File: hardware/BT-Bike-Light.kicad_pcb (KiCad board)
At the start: 2 copper layers, 0 parts

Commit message: Replace battery connector footprint and import footprints
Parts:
- added BT101: 18650, Keystone:254, F.Cu at (130.6, 129.6)
- added BZ101: Buzzer, PUI-Audio:PUI_AT-1220-TT-3V-2-R, F.Cu at (43.6, 112.8)
- added C101: 100nF, Capacitor_SMD:C_0402_1005Metric, F.Cu at (137.1, 86.0)
- added C102: 100nF, Capacitor_SMD:C_0402_1005Metric, F.Cu at (118.9, 100.1)
- added C103: 1uF, Capacitor_SMD:C_0402_1005Metric, F.Cu at (60.4, 123.1)
- added C104: 1uF, Capacitor_SMD:C_0402_1005Metric, F.Cu at (66.0, 123.1)
- added C201: 1uF, Capacitor_SMD:C_0402_1005Metric, F.Cu at (76.9, 75.0)
- added C202: 1uF, Capacitor_SMD:C_0402_1005Metric, F.Cu at (81.3, 75.0)
- added C301: 220nF, Capacitor_SMD:C_0402_1005Metric, F.Cu at (97.9, 95.0)
- added C302: 1uF, Capacitor_SMD:C_0402_1005Metric, F.Cu at (98.4, 96.6)
- added C401: 10uF, Capacitor_SMD:C_0402_1005Metric, F.Cu at (100.7, 116.2)
- added C402: 100nF, Capacitor_SMD:C_0402_1005Metric, F.Cu at (100.7, 115.1)
- added C403: 100nF, Capacitor_SMD:C_0402_1005Metric, F.Cu at (100.7, 114.0)
- added C501: 4.7uF, Capacitor_SMD:C_0402_1005Metric, F.Cu at (91.3, 76.3)
- added C502: 4.7uF, Capacitor_SMD:C_0402_1005Metric, F.Cu at (100.3, 75.9)
- added D501: RED, LED_SMD:LED_Cree-XP, F.Cu at (103.0, 77.0)
- added F101: 3A, Fuse:Fuse_1812_4532Metric, F.Cu at (85.5, 74.1)
- added J101: USB_C_Charge_Port, CUI-Devices:UJC-HP2-3-SMT-TR, F.Cu at (124.8, 83.6)
- added J102: SWD_Header, Samtech:FTSH-107-01-F-DV-K, F.Cu at (99.5, 85.3)
- added JP201: TIM_DISABLE, Jumper:SolderJumper-2_P1.3mm_Open_TrianglePad1.0x1.5mm, F.Cu at (83.5, 79.4)
- added Q101: DMN3731U-7, Package_TO_SOT_SMD:SOT-23, F.Cu at (52.5, 122.6)
- added R101: 10K, Resistor_SMD:R_0402_1005Metric, F.Cu at (135.0, 86.0)
- added R102: 5.1K, Resistor_SMD:R_0402_1005Metric, F.Cu at (123.8, 86.0)
- added R103: 5.1K, Resistor_SMD:R_0402_1005Metric, F.Cu at (125.9, 86.0)
- added R104: 10K, Resistor_SMD:R_0402_1005Metric, F.Cu at (113.7, 84.3)
- added R105: 10K, Resistor_SMD:R_0402_1005Metric, F.Cu at (113.7, 86.3)
- added R106: 1K, Resistor_SMD:R_0402_1005Metric, F.Cu at (49.3, 121.5)
- added R107: 1K, Resistor_SMD:R_0402_1005Metric, F.Cu at (49.3, 122.6)
- added R201: 10K, Resistor_SMD:R_0402_1005Metric, F.Cu at (83.2, 81.4)
- added R202: 1K, Resistor_SMD:R_0402_1005Metric, F.Cu at (79.8, 79.9)
- added R301: 200K, Resistor_SMD:R_0603_1608Metric, F.Cu at (91.5, 95.2)
- added R302: 0.01, Resistor_SMD:R_0603_1608Metric, F.Cu at (98.2, 98.8)
- added R303: 1K, Resistor_SMD:R_0402_1005Metric, F.Cu at (99.1, 95.0)
- added R501: 0.067, Resistor_SMD:R_0402_1005Metric, F.Cu at (100.3, 78.2)
- added SW101: Button, Button_Switch_THT:SW_Tactile_SPST_Angled_PTS645Vx58-2LFS, F.Cu at (133.6, 80.2)
- added TH201: 10K, Resistor_SMD:R_0402_1005Metric, F.Cu at (82.8, 77.5)
- added U101: BC805M, Fanstel:BC805M, F.Cu at (106.9, 94.1)
- added U102: TPS7A02, Package_TO_SOT_SMD:SOT-23-5, F.Cu at (63.2, 123.6)
- added U201: MCP73834-xxx-MF, Package_DFN_QFN:DFN-10-1EP_3x3mm_P0.5mm_EP1.58x2.35mm, F.Cu at (79.1, 77.5)
- added U301: STC3100IQT, Package_DFN_QFN:DFN-8-1EP_3x3mm_P0.5mm_EP1.7x2.4mm, F.Cu at (95.0, 96.6)
- added U401: LIS2DTW12, Package_LGA:LGA-12_2x2mm_P0.5mm, F.Cu at (98.2, 115.4)
- added U501: PAM2808, Package_SO:Diodes_SO-8EP, F.Cu at (96.1, 77.0)

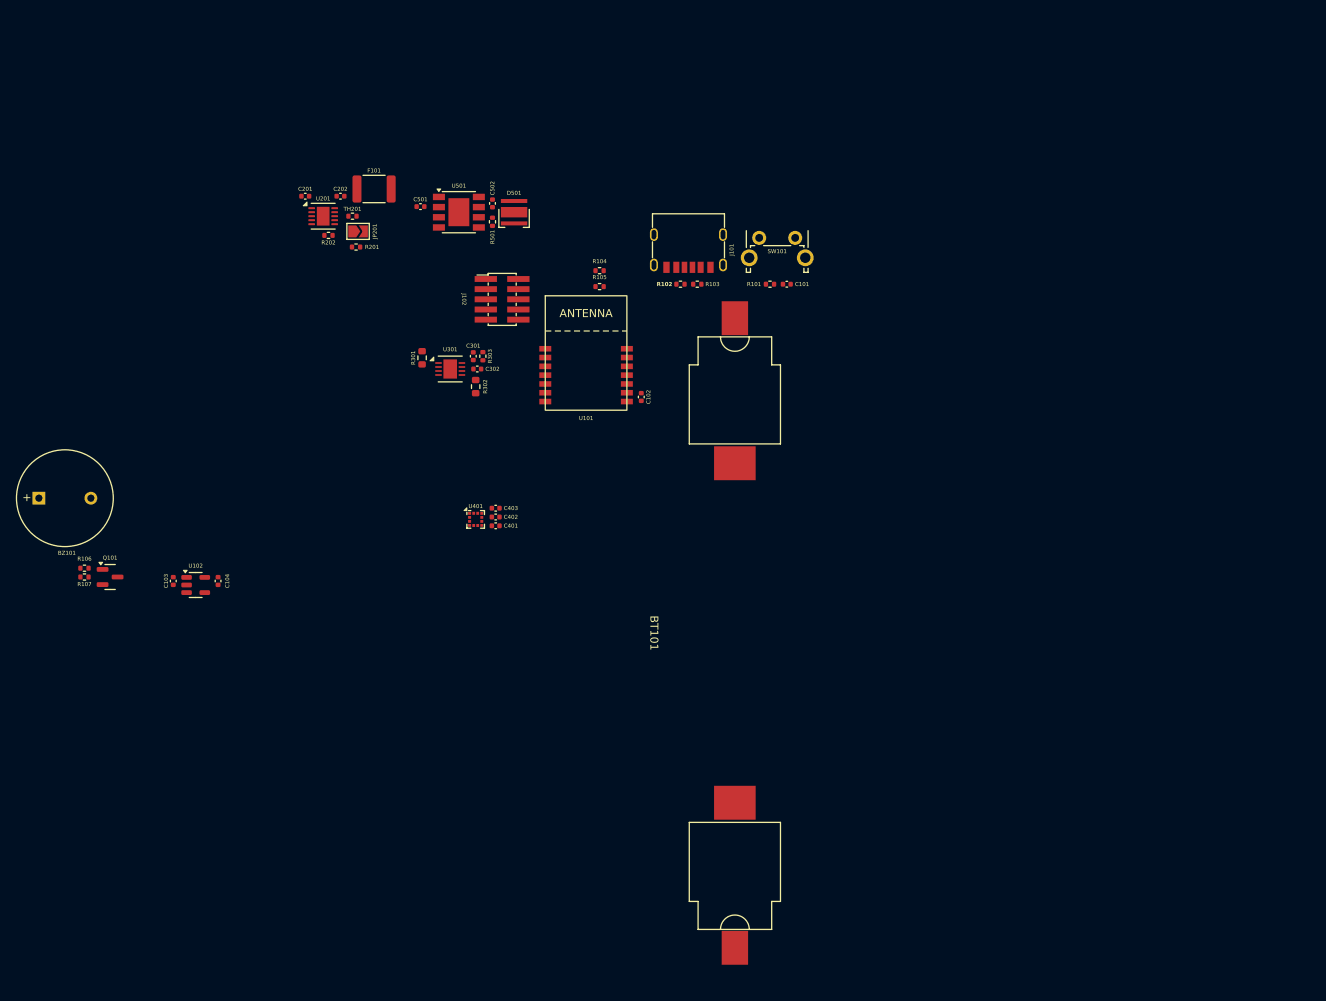
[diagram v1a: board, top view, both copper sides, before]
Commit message: Add battery protection and swap some connectors
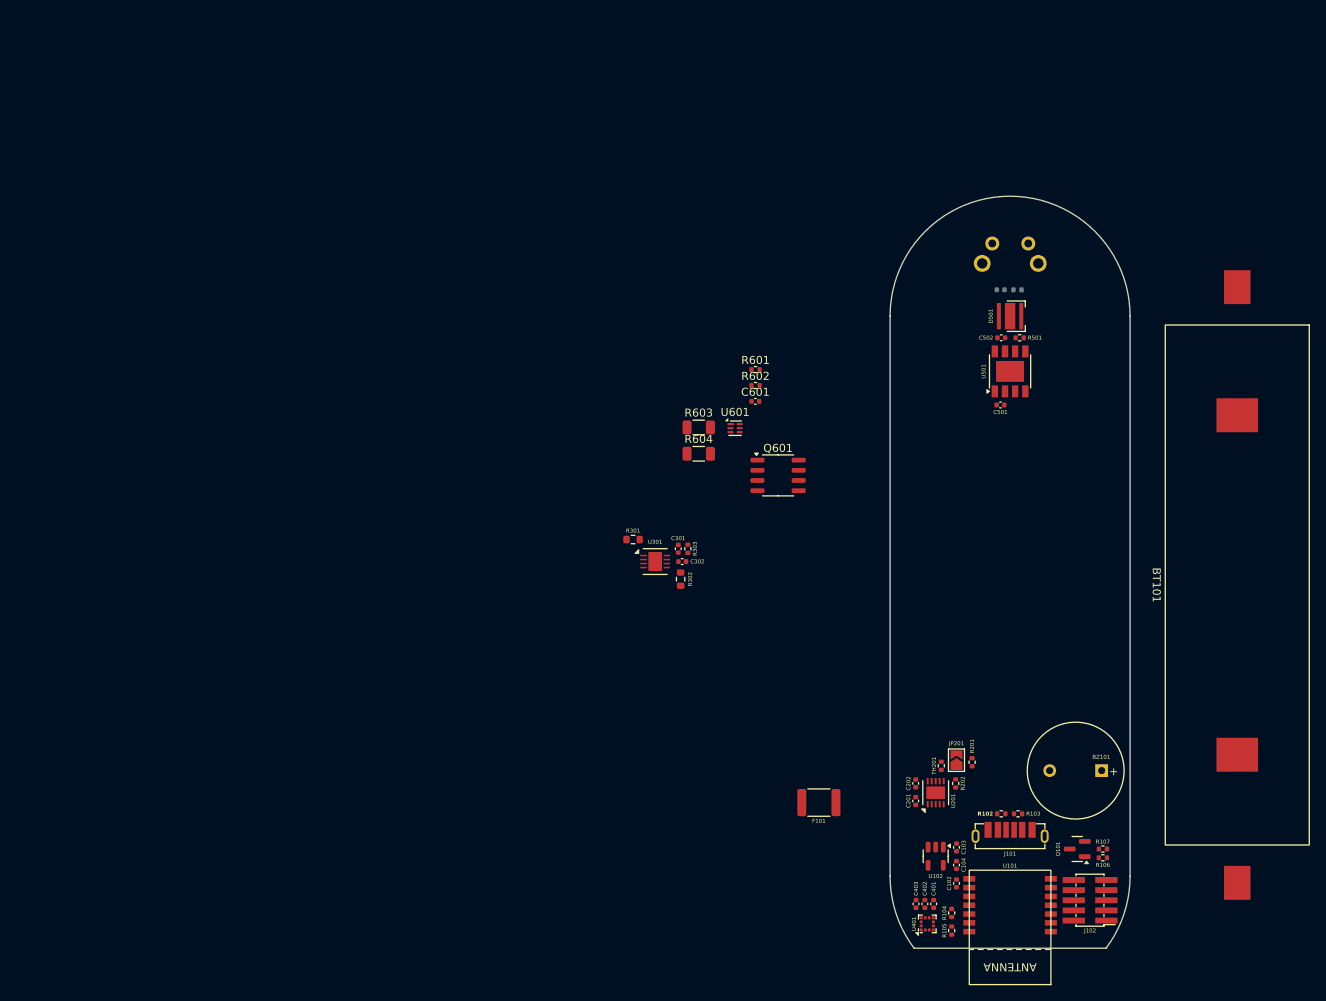
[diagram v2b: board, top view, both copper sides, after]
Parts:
- added C601: 100nF, Capacitor_SMD:C_0402_1005Metric, F.Cu at (133.2, 100.6)
- added Q601: DSG/CHG, Package_SO:SO-8_3.9x4.9mm_P1.27mm, F.Cu at (136.0, 109.9)
- added R601: 330, Resistor_SMD:R_0402_1005Metric, F.Cu at (133.2, 96.7)
- added R602: 2.2K, Resistor_SMD:R_0402_1005Metric, F.Cu at (133.2, 98.7)
- added R603: 5M, Resistor_SMD:R_1206_3216Metric, F.Cu at (126.1, 103.9)
- added R604: 5M, Resistor_SMD:R_1206_3216Metric, F.Cu at (126.1, 107.2)
- added U601: BQ297xy, Package_SON:WSON-6_1.5x1.5mm_P0.5mm, F.Cu at (130.6, 104.0)
- C101, R101, SW101: moved to B.Cu
- J101: footprint CUI-Devices:UJC-HP2-3-SMT-TR -> Molex:2171780001
- R302: value 0.01 -> 0.03
- moved BZ101 137.1 mm to (176.4, 146.8), turned to 180 degrees
- moved R106 132.3 mm to (176.6, 157.7), turned to 180 degrees
- moved R107 131.8 mm to (176.6, 156.6), turned to 180 degrees
- moved Q101 125.6 mm to (173.4, 156.6), turned to 180 degrees
- moved J102 111.6 mm to (177.0, 165.6), turned to 90 degrees
- moved C201 107.4 mm to (153.2, 150.6), turned to -90 degrees
- moved U201 105.1 mm to (155.7, 149.6), turned to 90 degrees
- moved R202 104.1 mm to (158.2, 148.4), turned to -90 degrees
- moved C103 103.4 mm to (158.3, 156.4)
- moved C202 102.7 mm to (153.2, 148.4), turned to -90 degrees
- moved TH201 100.7 mm to (156.4, 146.2), turned to 90 degrees
- moved R201 100.4 mm to (160.3, 145.8), turned to 90 degrees
- moved JP201 99.8 mm to (158.3, 145.5), turned to 90 degrees
- moved C104 98.9 mm to (158.3, 158.6), turned to 90 degrees
- moved U102 98.5 mm to (155.7, 157.5), turned to -90 degrees
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- renumbered R105 to R104, R104 to R105
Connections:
- BZ101 pad 1: Net-(BZ101-+) -> +BATT
- C501 pad 1: Net-(U501-VIN) -> +BATT
- R104 pad 2: /SCL -> /SDA
- R105 pad 2: /SDA -> /SCL
- R107 pad 1: Net-(BZ101-+) -> +BATT
- U101 pad 10: unconnected-(U101-P005-Pad10) -> /CHRG_STAT2
- U101 pad 11: unconnected-(U101-P014-Pad11) -> /CHRG_STAT1
- U101 pad 12: unconnected-(U101-P004-Pad12) -> /ACCEL_INT1
- U101 pad 13: unconnected-(U101-P000-Pad13) -> /SDA
- U101 pad 14: unconnected-(U101-P001-Pad14) -> /SCL
- U101 pad 3: unconnected-(U101-P020-Pad3) -> /ACCEL_INT2
- U501 pad 2: Net-(U501-VIN) -> +BATT
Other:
- board outline added: 30 x 94 mm

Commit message: Finish pin assignments
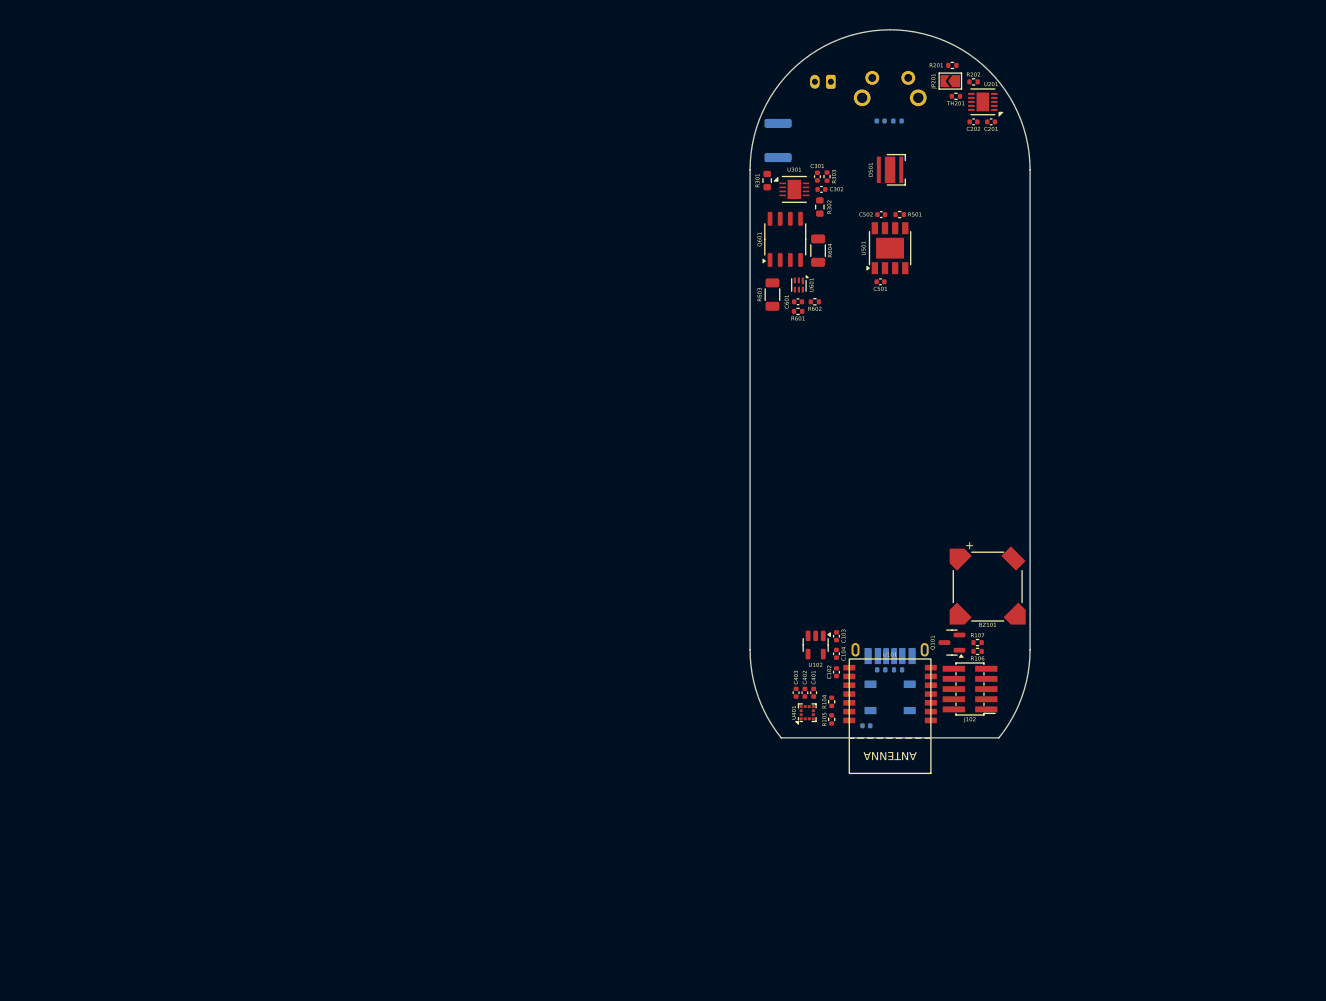
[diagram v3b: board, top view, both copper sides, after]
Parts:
- added C105: 100nF, Capacitor_SMD:C_0402_1005Metric, B.Cu at (147.0, 141.2)
- added D101: WS2812B, LED_SMD:LED_WS2812B_PLCC4_5.0x5.0mm_P3.2mm, B.Cu at (150.0, 137.7)
- BT101: footprint Keystone:254 -> Connector_JST:JST_PH_S2B-PH-K_1x02_P2.00mm_Horizontal; moved to B.Cu
- BZ101: footprint PUI-Audio:PUI_AT-1220-TT-3V-2-R -> PUI-Audio:SMT-0827-S-HT-R
- F101, J101, R102, R103: moved to B.Cu
- moved R202 87.7 mm to (160.4, 60.7), turned to 0 degrees
- moved R201 87.1 mm to (157.8, 58.7), turned to 180 degrees
- moved U201 86.6 mm to (161.6, 63.2), turned to 180 degrees
- moved C201 85.4 mm to (162.6, 65.7), turned to 0 degrees
- moved JP201 84.9 mm to (157.5, 60.6), turned to 180 degrees
- moved TH201 83.7 mm to (158.2, 62.5), turned to 180 degrees
- moved C202 83.0 mm to (160.4, 65.7), turned to 0 degrees
- moved F101 82.9 mm to (136.0, 68.0), turned to -90 degrees
- moved BT101 80.9 mm to (142.6, 60.7), turned to 180 degrees
- moved R302 49.7 mm to (141.2, 76.3)
- moved R303 49.7 mm to (142.1, 72.5)
- moved C301 49.7 mm to (140.9, 72.5)
- moved C302 49.7 mm to (141.4, 74.2)
- moved U301 49.7 mm to (138.0, 74.2)
- moved R301 47.9 mm to (134.6, 73.0), turned to -90 degrees
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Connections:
- net /Battery Charger/VBUS renamed +5V
- J102 pad 10: /nRST -> unconnected-(J102-~{RESET}-Pad10)
- U101 pad 10: /CHRG_STAT2 -> /LED_EN
- U101 pad 11: /CHRG_STAT1 -> /BTN
- U101 pad 4: /nRST -> /LED_STAT
- U101 pad 5: unconnected-(U101-P018-Pad5) -> /BUZZER
- U101 pad 6: unconnected-(U101-P016-Pad6) -> /CHRG_STAT2
- U101 pad 7: unconnected-(U101-P012-Pad7) -> /CHRG_STAT1
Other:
- board size 30 x 94 mm -> 35 x 88.5 mm
